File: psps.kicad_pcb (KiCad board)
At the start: 2 copper layers, 20 x 30 mm, 27 parts, among them J1 USB_C_Receptacle, J2 Conn_01x03, U1 TLV62585, U2 TLV61046ADB

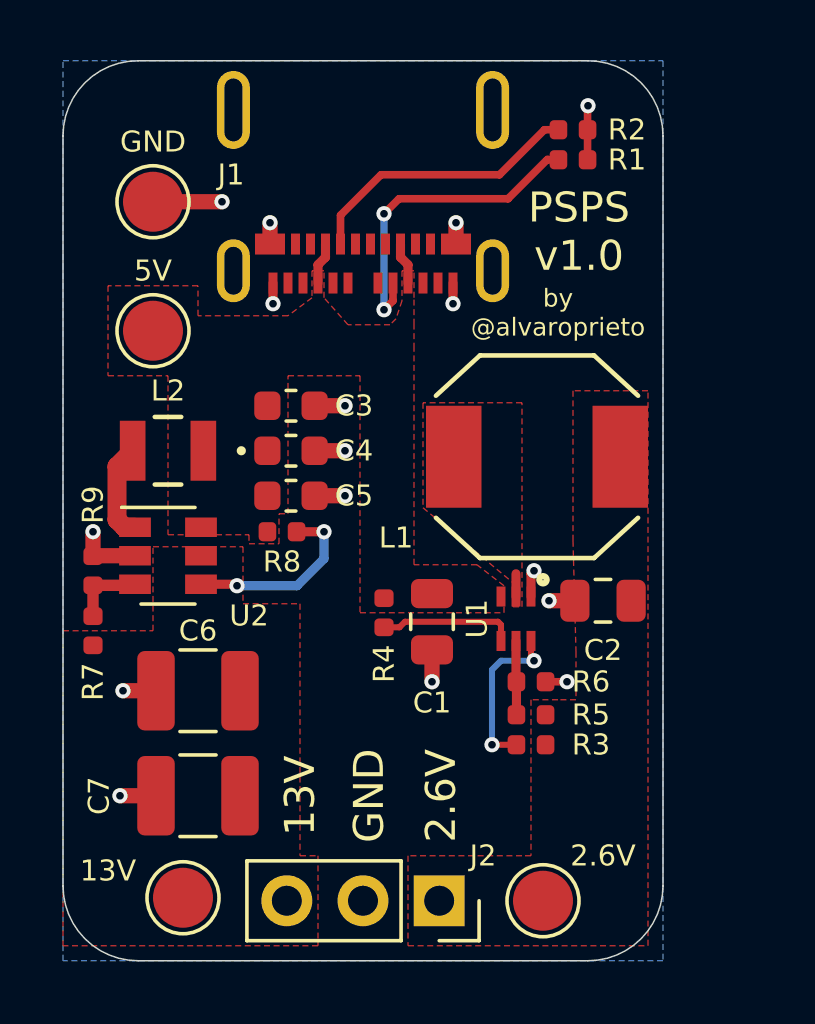
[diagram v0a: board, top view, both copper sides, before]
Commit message: Released PSPS 1.1 to oshpark
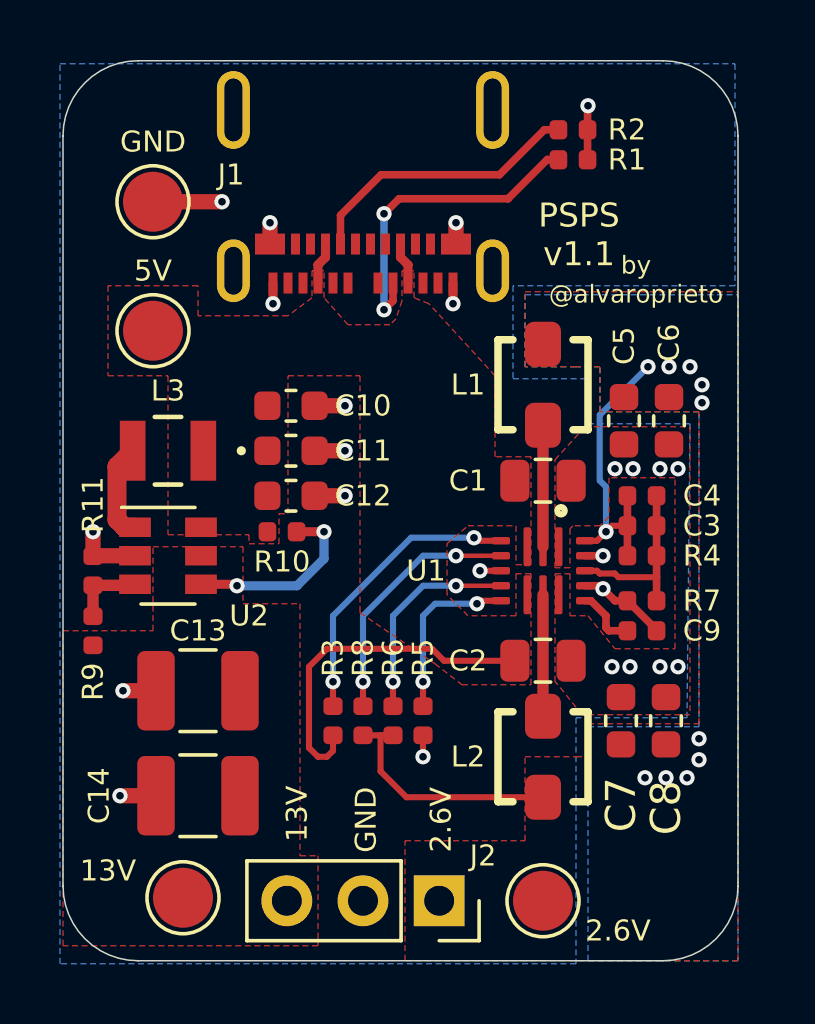
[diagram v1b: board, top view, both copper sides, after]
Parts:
- removed the REF** at (110.0, 55.0)
- added C3: 18pF, Capacitor_SMD:C_0402_1005Metric, F.Cu at (119.3, 55.5)
- added C4: 18pF, Capacitor_SMD:C_0402_1005Metric, F.Cu at (119.3, 54.5)
- added C5: 22uF, Capacitor_SMD:C_0603_1608Metric, F.Cu at (118.7, 52.0)
- added C6: 22uF, Capacitor_SMD:C_0603_1608Metric, F.Cu at (120.2, 52.0)
- added C7: 22uF, Capacitor_SMD:C_0603_1608Metric, F.Cu at (118.6, 62.0)
- added C8: 22uF, Capacitor_SMD:C_0603_1608Metric, F.Cu at (120.1, 62.0)
- added C9: 5.6nF, Capacitor_SMD:C_0402_1005Metric, F.Cu at (119.3, 59.0)
- added L2: 470 nH, alvarop:IHLP1212AEERR47M11, F.Cu at (116.0, 63.2)
- added R7: 120k, Resistor_SMD:R_0402_1005Metric, F.Cu at (119.3, 58.0)
- added R8: 402k, Resistor_SMD:R_0402_1005Metric, F.Cu at (110.0, 62.0)
- added REF**: OSHW-Logo2_7.3x6mm_SilkScreen, Symbol:OSHW-Logo2_7.3x6mm_SilkScreen, B.Cu at (118.5, 43.5)
- C1: value 10uF -> 22uF
- L1: value 1uH -> 470 nH; footprint ultra_librarian:SPM6530T-1R0M120 -> alvarop:IHLP1212AEERR47M11
- R3: value 1M -> 0
- R4: value 0 -> 402k
- R5: value 332k -> 0
- R6: value 100k -> 402k
- U1: value TLV62585 -> TPS62480; footprint alvarop:TLV62585PDRLR -> alvarop:TPS62480
- moved R4 8.81 mm to (119.3, 56.5), turned to 0 degrees
- moved R3 6.65 mm to (109.0, 62.0), turned to 90 degrees
- moved C1 5.98 mm to (116.0, 54.0), turned to 0 degrees
- moved R6 4.78 mm to (111.0, 62.0), turned to 270 degrees
- moved R5 3.61 mm to (112.0, 62.0), turned to 270 degrees
- moved C2 2.83 mm to (116.0, 60.0), turned to 0 degrees
- moved L1 2.41 mm to (116.0, 50.8), turned to 90 degrees
- moved U1 1.84 mm to (116.0, 57.0)
- renumbered C3 to C10, C4 to C11, C5 to C12, C6 to C13, C7 to C14, L2 to L3, R8 to R10, R9 to R11, R7 to R9
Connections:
- C2 pad 1: /2V6 -> +5V
- R3 pad 1: /2V6 -> +5V
- R4 pad 1: Net-(R4-Pad1) -> /2V6
- R4 pad 2: +5V -> Net-(C3-Pad2)
- R5 pad 2: /2V6 -> GND
- R6 pad 1: GND -> Net-(R6-Pad1)
- R6 pad 2: Net-(R5-Pad1) -> /2V6
- U1 pad 4: Net-(R4-Pad1) -> Net-(R3-Pad2)
- U1 pad 5: Net-(R5-Pad1) -> Net-(R8-Pad1)
- U1 pad 6: Net-(R3-Pad2) -> GND
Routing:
- net /2V6: track 0.00 -> 17.8 mm, vias 0 -> 11
- net +5V: track 2.81 -> 14.3 mm
- net Net-(R8-Pad1): track 0.00 -> 8.44 mm, vias 0 -> 2
- net Net-(R6-Pad1): track 0.00 -> 7.03 mm, vias 0 -> 2
- net Net-(C3-Pad2): track 0.00 -> 5.97 mm
- net Net-(R4-Pad1): track 4.56 -> 0.00 mm
- net Net-(R3-Pad2): track 5.54 -> 9.73 mm
- net Net-(L2-Pad1): track 0.00 -> 4.05 mm
- net Net-(R5-Pad1): track 2.47 -> 5.82 mm, vias 0 -> 2
- net Net-(L1-Pad1): track 0.76 -> 4.05 mm
- net Net-(C9-Pad1): track 0.00 -> 2.06 mm
- net GND: track 18.0 -> 19.5 mm, vias 16 -> 24
- added copper zone on B.Cu, net /2V6
- added copper zone on F.Cu, net GND
- removed copper zone on F.Cu, net Net-(L1-Pad1)
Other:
- board size 20 x 30 mm -> 22.5 x 30 mm
- board text added: "PSPS v1.1"
- board text removed: "PSPS v1.0"
